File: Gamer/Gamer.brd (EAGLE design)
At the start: 168.9 x 63.5 mm, 44 parts, among them J1 HEADER-1X8, J2 HEADER-1X8, J3 HEADER-1X8, J4 HEADER-1X8, J5 HEADER-1X8, J6 HEADER-1X8, J7 HEADER-1X8, J8 HEADER-1X8, U1 MMA8653FCR1, U2 ATTINY48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

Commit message: gamer - more manual routing
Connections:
- net EEE renamed GND
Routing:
- net 25: track 0.00 -> 135.4 mm, vias 0 -> 1
- net 23: track 0.00 -> 131.0 mm, vias 0 -> 1
- net 24: track 0.00 -> 119.3 mm
- net 27: track 0.00 -> 111.5 mm
- net 22: track 0.00 -> 107.0 mm
- net 18: track 0.00 -> 100.9 mm
- net N$34: track 0.00 -> 3.33 mm
- net 3V3: track 0.00 -> 2.13 mm

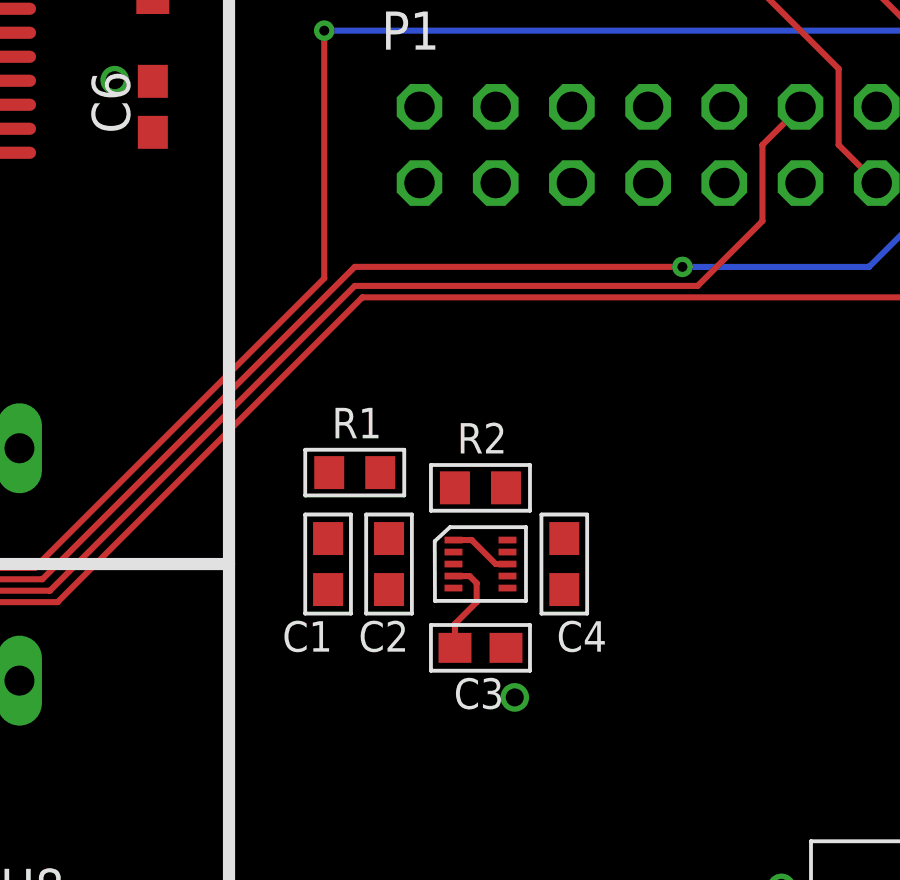
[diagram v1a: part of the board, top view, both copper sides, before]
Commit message: gamer - hand route accelerometer
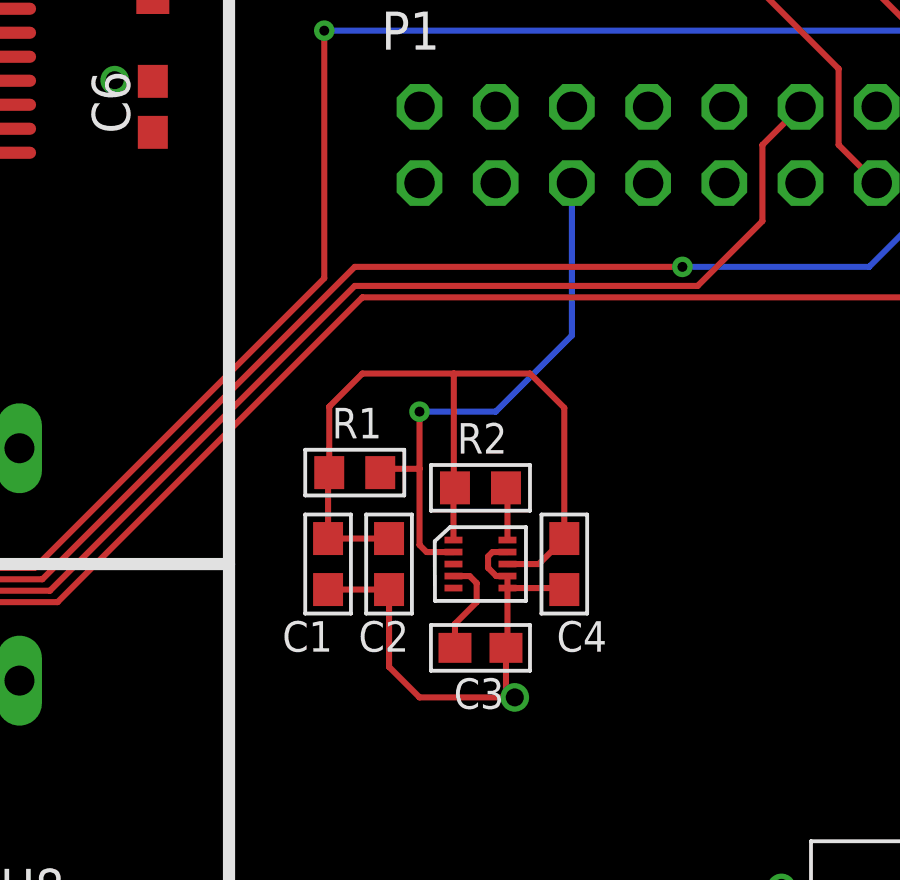
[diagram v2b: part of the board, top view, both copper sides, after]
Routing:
- net 3V3: track 2.13 -> 27.4 mm
- net 3/SCL: track 0.00 -> 18.6 mm, vias 0 -> 1
- net GND: track 0.00 -> 17.2 mm
- net 2/SDA: track 0.00 -> 1.76 mm

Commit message: gamer - auto route 100%
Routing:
- net 3V3: track 27.4 -> 328.0 mm, vias 0 -> 13
- net 8/CE0: track 0.00 -> 183.5 mm, vias 0 -> 6
- net 11/SCLK: track 0.00 -> 172.0 mm, vias 0 -> 5
- net MOSI3/MISO4: track 0.00 -> 154.7 mm, vias 0 -> 2
- net MOSI2/MISO3: track 0.00 -> 107.8 mm, vias 0 -> 3
- net M3_RESET: track 0.00 -> 94.8 mm, vias 0 -> 4
- net 9/MISO: track 0.00 -> 94.1 mm, vias 0 -> 2
- net MOSI1/MISO2: track 0.00 -> 93.4 mm, vias 0 -> 3
- net M4_RESET: track 0.00 -> 86.2 mm, vias 0 -> 2
- net 10/MISO: track 0.00 -> 84.7 mm, vias 0 -> 2
- net GND: track 17.2 -> 82.0 mm
- net M1_RESET: track 0.00 -> 64.8 mm, vias 0 -> 3
- net M1_COL1: track 0.00 -> 54.1 mm
- net M2_COL0: track 0.00 -> 45.8 mm
- net M3_COL0: track 0.00 -> 42.9 mm
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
